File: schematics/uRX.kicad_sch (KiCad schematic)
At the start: 70 parts, among them J1 RF_In, J2 AudioJack2_Ground, J5 +5V, J6 RF_In, U1 CBT3253, U2 LM4562, U3 ESP32-DEVKIT, U4 Si5351A-B-GT, U5 OPA2690, U6 Si4732-A10, U7 PCM1808PWR, U8 LM4040-2.5, Y1 25MHz, Y2 32768kHz

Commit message: schematics finalization
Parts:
- removed C10, C11, C12: 100n, Capacitor_THT:C_Disc_D6.0mm_W2.5mm_P5.00mm, symbol Device:C_Small
- removed J2: AudioJack2_Ground, symbol Connector_Audio:AudioJack2_Ground
- removed L1, L2: Ferrite_perl, symbol Device:L_Ferrite_Small
- removed unit 3 of U2
- added C29: 10u, Capacitor_SMD:C_0603_1608Metric, symbol Device:C_Small
- added C30, C31: 100n, Capacitor_SMD:C_0603_1608Metric, symbol Device:C_Small
- added J3: AudioJack2_Ground, symbol Connector_Audio:AudioJack2_Ground
- added J4: +5Vfiltered, Connector_Pin:Pin_D0.9mm_L10.0mm_W2.4mm_FlatFork, symbol Connector_Generic:Conn_01x01
- added J7: +3.3Vfiltered, Connector_Pin:Pin_D0.9mm_L10.0mm_W2.4mm_FlatFork, symbol Connector_Generic:Conn_01x01
- added L5, L6: Ferrite_perl, Inductor_SMD:L_0603_1608Metric, symbol Device:L_Ferrite_Small
- added R22, R23, R24: 22, Resistor_SMD:R_0603_1608Metric, symbol Device:R
- added Rf1: 33, Resistor_SMD:R_0603_1608Metric, symbol Device:R
- added U9: PCM1808PWR, PW14, symbol 2026-01-28_13-06-42:PCM1808PWR
- C1, C13, C14, C17, C18, C20, C21, C22, C23, C25, C28, C8, C9: footprint Capacitor_THT:C_Disc_D3.8mm_W2.6mm_P2.50mm -> Capacitor_SMD:C_0603_1608Metric
- C15, C16, C19, C2, C24, C26, C27, C3, C4, C5: footprint Capacitor_THT:C_Disc_D6.0mm_W2.5mm_P5.00mm -> Capacitor_SMD:C_0603_1608Metric
- R1, R10, R11, R12, R13, R14, R16, R18, R19, R2, R20, R21, R3, R4, R5, R6, R8, Rf10, Rf8: footprint Resistor_THT:R_Axial_DIN0207_L6.3mm_D2.5mm_P10.16mm_Horizontal -> Resistor_SMD:R_0603_1608Metric
- U2, U5: footprint Package_DIP:DIP-8_W7.62mm_Socket_LongPads -> SOIC-8
- U6: footprint Package_SO:SOIC-16_3.9x9.9mm_P1.27mm -> Package_SO:SOIC-8_3.9x4.9mm_P1.27mm
- renumbered Rg10DNP to Rg10DNP1, Rg8DNP to Rg8DNP1
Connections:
- net +3.3V: now also L5.1; no longer U6.14 (VDD)
- net +5V: now also L6.1; no longer R20.2, U1.16 (VCC)
- net GND: now also C29.1, C30.1, C31.1, U9.10 (MD0), U9.11 (MD1), U9.12 (FMT), U9.2 (AGND), U9.5 (DGND); no longer C23.2, C28.2, U7.3 (VCC), U7.4 (VDD)
- net SCL: now also U6.11 (SCLK)
- net SDA: now also U6.12 (SDIO)
- net at C18.1: now also J3.S, U9.13 (VINL)
- net at C17.1: now also J3.T, U9.14 (VINR)
- net I2S0_DOUT: now reaches R21.2
- net I2S0_DOUT: now also U3.21 (D32)
- net at U4.6 (CLK2): now also Rf1.2; no longer U7.6 (SCKI)
- net I2S1_DOUT: now reaches U3.15 (D23)
- net I2S1_DOUT: now also R24.2
- net I2S1_LRCK: now reaches U3.23 (D25)
- net I2S1_LRCK: now also R22.2
- net I2S1_BCK: now reaches U3.24 (D26)
- net I2S1_BCK: now also R23.2
- net I2S0_BCK: now reaches U3.26 (D14)
- net I2S0_BCK: now also R2.2
- net I2S0_LRCK: now reaches U3.3 (D15)
- net I2S0_LRCK: now also R1.2
- net Pin8 V+ renamed +5Vfiltered
- net +5Vfiltered: now also C28.2, R20.2, U1.16 (VCC), U7.3 (VCC), C31.2, U9.3 (VCC)
- new net: J7.1 (Pin_1), L5.2
- new net: J4.1 (Pin_1), L6.2
- new net: R23.1, U9.8 (BCK)
- new net: C29.2, U9.1 (VREF)
- new net: R24.1, U9.9 (DOUT)
- new net: Rf1.1, U7.6 (SCKI), U9.6 (SCKI)
- new net: R22.1, U9.7 (LRCK)
- new net +3.3Vfiltered: C23.2, C30.2, U6.14 (VDD), U7.4 (VDD), U9.4 (VDD)
- no-connect marks 24 -> 17
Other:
- moved on the sheet: C17, C18, C20, C23, C25, C26, C27, C28, J6, R1, R2, R21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

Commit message: add usb power
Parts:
- removed R6: 10k, Resistor_SMD:R_0603_1608Metric, symbol Device:R
- added Bat1+: Bat1-, JST-XH, symbol Connector:Conn_01x02_Socket
- added Bat2+: Bat2-, JST-XH, symbol Connector:Conn_01x02_Socket
- added C10, C12: 2.2u, Capacitor_SMD:C_0603_1608Metric, symbol Device:C_Small
- added C11: 100n, Capacitor_SMD:C_0603_1608Metric, symbol Device:C_Small
- added D1: LED_Small, symbol Device:LED_Small
- added P1: USB_C_Plug_USB2.0, symbol Connector:USB_C_Plug_USB2.0
- added R25: 10kΩ, Resistor_SMD:R_0603_1608Metric, symbol Device:R_Small
- added R26, R6: 4.7kΩ, Resistor_SMD:R_0603_1608Metric, symbol Device:R_Small
- added Rf2, Rf3: 47, Resistor_SMD:R_0603_1608Metric, symbol Device:R
- added U11: IP2326, Package_DFN_QFN:QFN-24-1EP_4x4mm_P0.5mm_EP2.7x2.7mm, symbol uRX:STUSB4500QTR
- C25: value ... -> 100p
- C8, C9: value 1n -> 2.2u
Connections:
- net +3.3Vfiltered: now also R5.1
- net +5Vfiltered: now also C10.1, C11.1
- net GND: now also C9.2, C10.2, C11.2, C12.2, D1.1 (K), R25.2, R26.2, R6.2, U11.18 (PGND); no longer U7.11 (MD1), U9.11 (MD1)
- net at U3.19 (D34), U6.9 (RST): now also R5.2
- net at U3.5 (D4): no longer C9.2
- net VRev2.5: now reaches C26.1, C27.1, R18.2, R19.2, R20.1, U8.4 (K)
- new net: P1.A1 (GND), P1.A12 (GND), P1.B1 (GND), P1.B12 (GND)
- new net: P1.A4 (VBUS), P1.A9 (VBUS), P1.B4 (VBUS), P1.B9 (VBUS)
- new net: P1.A6 (D+), U11.2 (DP)
- new net: P1.A7 (D-), U11.1 (DM)
- new net: Rf2.1, U1.2 (S1)
- new net: Rf2.2, U4.9 (CLK1)
- new net: R26.1, U11.11 (ISET)
- new net: Bat1+.2 (Pin_2), Bat2+.2 (Pin_2), C9.1, U11.21 (VOUT), U11.22 (VOUT)
- new net: Bat1+.1 (Pin_1), Bat2+.1 (Pin_1)
- new net: D1.2 (A), U11.6 (LED)
- new net: R6.1, U11.3 (VSET)
- new net: Rf3.2, U4.10 (CLK0)
- new net: R25.1, U11.4 (NTC)
- new net: C12.1, U11.19 (VSYS), U11.20 (VSYS)
- new net: U11.25 (GND), U11.8 (VIN_UVSET)
- new net: Rf3.1, U1.14 (S0)
- now unconnected: C8.1, C8.2, U3.9 (D18)
- no-connect marks 17 -> 15
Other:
- moved on the sheet: C16, C25, C26, C27, C5, R10, R20, U8

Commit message: finalize power circuit
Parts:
- removed Bat1+: Bat1-, JST-XH, symbol Connector:Conn_01x02_Socket
- removed Bat2+: Bat2-, JST-XH, symbol Connector:Conn_01x02_Socket
- removed C9: 2.2u, Capacitor_SMD:C_0603_1608Metric, symbol Device:C_Small
- added Bat0, Bat1: JST-XH, symbol Connector_Generic:Conn_01x03
- added C32: 100n, Capacitor_SMD:C_0603_1608Metric, symbol Device:C_Small
- added C33: 4.7n, Capacitor_SMD:C_0603_1608Metric, symbol Device:C_Small
- added D2: LED_Small, symbol Device:LED_Small
- added L1: 2.2uH,50mA, PCM_JLCPCB:L_0805, symbol PCM_JLCPCB-Inductors:1uH,50mA
- added R27, R33: 100, Resistor_SMD:R_0603_1608Metric, symbol Device:R_Small
- added R28: 0.5, Resistor_SMD:R_0603_1608Metric, symbol Device:R_Small
- added R29: 5.1K, Resistor_SMD:R_0603_1608Metric, symbol Device:R_Small
- added R30: 51k, Resistor_SMD:R_0603_1608Metric, symbol Device:R_Small
- added R31, R32: 120K, Resistor_SMD:R_0603_1608Metric, symbol Device:R_Small
- added R4: 100, Resistor_SMD:R_0603_1608Metric, symbol Device:R
- C12, C8: value 2.2u -> 10u
- R25: value 10kΩ -> 1M
- R26: value 4.7kΩ -> 60K
- R6: value 4.7kΩ -> 5.1kΩ
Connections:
- net GND: now also C8.2, P1.A1 (GND), P1.A12 (GND), P1.B1 (GND), P1.B12 (GND), U11.24 (VBAT_GND), Bat0.1 (Pin_1), Bat1.1 (Pin_1), C33.2, D2.1 (K), R29.2, R30.2, R31.2, R32.2
- net at P1.A4 (VBUS), P1.A9 (VBUS), P1.B4 (VBUS)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: now also R28.1
- net at P1.A5 (CC): now also R6.1
- net at P1.S1 (SHIELD): now also R25.1, C33.1
- net at U11.21 (VOUT), U11.22 (VOUT): now also Bat0.3 (Pin_3), Bat1.3 (Pin_3)
- net at D1.2 (A): now also R27.2; no longer U11.6 (LED)
- net at U11.3 (VSET): no longer R6.1
- net at U11.4 (NTC): now also R30.1; no longer R25.1
- net at U11.13 (VIN): now also C8.1, L1.2, R28.2, R29.1
- net at U11.14 (BST): now also C32.2
- net at U11.15 (LX): now also U11.17 (LX)
- net at U11.16 (LX): now also C32.1, L1.1
- net at U11.23 (VBATM): now also R4.1
- net at U11.25 (GND), U11.8 (VIN_UVSET): now also R32.1
- net at U11.5 (BAT_STAT): now also R33.1
- net at U11.9 (VIN_OVSET): now also R31.1
- new net: Bat0.2 (Pin_2), Bat1.2 (Pin_2), R4.2
- new net: R27.1, U11.6 (LED)
- new net: D2.2 (A), R33.2
- no-connect marks 15 -> 19
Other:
- moved on the sheet: C12, C8, P1, R26

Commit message: add power to the rest
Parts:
- removed Bat0, Bat1: JST-XH, symbol Connector_Generic:Conn_01x03
- removed C12: 10u, Capacitor_SMD:C_0603_1608Metric, symbol Device:C_Small
- removed C25: 100p, Capacitor_SMD:C_0603_1608Metric, symbol Device:C_Small
- removed C32: 100n, Capacitor_SMD:C_0603_1608Metric, symbol Device:C_Small
- removed C33: 4.7n, Capacitor_SMD:C_0603_1608Metric, symbol Device:C_Small
- removed D1, D2: LED_Small, symbol Device:LED_Small
- removed J6: RF_In, Connector_Pin:Pin_D0.9mm_L10.0mm_W2.4mm_FlatFork, symbol Connector_Generic:Conn_01x01
- removed JP1: Conn_01x02_Male, Connector_PinHeader_2.00mm:PinHeader_1x02_P2.00mm_Vertical, symbol Connector:Conn_01x02_Male
- removed L1: 2.2uH,50mA, PCM_JLCPCB:L_0805, symbol PCM_JLCPCB-Inductors:1uH,50mA
- removed P1: USB_C_Plug_USB2.0, symbol Connector:USB_C_Plug_USB2.0
- removed R15: 2.0kΩ, Resistor_SMD:R_0603_1608Metric, symbol Device:R_Small
- removed R25: 1M, Resistor_SMD:R_0603_1608Metric, symbol Device:R_Small
- removed R26: 60K, Resistor_SMD:R_0603_1608Metric, symbol Device:R_Small
- removed R27, R33: 100, Resistor_SMD:R_0603_1608Metric, symbol Device:R_Small
- removed R28: 0.5, Resistor_SMD:R_0603_1608Metric, symbol Device:R_Small
- removed R29: 5.1K, Resistor_SMD:R_0603_1608Metric, symbol Device:R_Small
- removed R30: 51k, Resistor_SMD:R_0603_1608Metric, symbol Device:R_Small
- removed R31, R32: 120K, Resistor_SMD:R_0603_1608Metric, symbol Device:R_Small
- removed R4: 100, Resistor_SMD:R_0603_1608Metric, symbol Device:R
- removed R6: 5.1kΩ, Resistor_SMD:R_0603_1608Metric, symbol Device:R_Small
- removed R9: 10kΩ, Resistor_SMD:R_0603_1608Metric, symbol Device:R_Small
- removed U11: IP2326, Package_DFN_QFN:QFN-24-1EP_4x4mm_P0.5mm_EP2.7x2.7mm, symbol uRX:STUSB4500QTR
- added Bat2, Bat3: JST-XH, Connector_JST:JST_XH_B3B-XH-A_1x03_P2.50mm_Vertical, symbol uRX:Conn_01x03
- added C34, C36, C37: 10u, Capacitor_SMD:C_0603_1608Metric, symbol uRX:C_Small
- added C35: 100n, Capacitor_SMD:C_0603_1608Metric, symbol uRX:C_Small
- added C9: 4.7n, Capacitor_SMD:C_0603_1608Metric, symbol uRX:C_Small
- added D3, D4: LED_Small, LED_SMD:L_0603_1608Metric, symbol uRX:LED_Small
- added J2: USB_C_Receptacle_USB2.0_14P, C165948, symbol uRX:USB_C_Receptacle_USB2.0_14P
- added J8: RF_In, Connector_Pin:Pin_D0.9mm_L10.0mm_W2.4mm_FlatFork, symbol Connector_Generic:Conn_01x01
- added L2: 2.2uH,3A, Inductor_SMD:L_4.0x4.0_H1.8, symbol uRX:1uH,50mA
- added R34: 1M, Resistor_SMD:R_0603_1608Metric, symbol uRX:R_Small
- added R35, R36, R44: 5.1K, Resistor_SMD:R_0603_1608Metric, symbol uRX:R_Small
- added R37: 33k, Resistor_SMD:R_0603_1608Metric, symbol uRX:R_Small
- added R38, R40: 100, Resistor_SMD:R_0603_1608Metric, symbol uRX:R_Small
- added R39: 100, Resistor_SMD:R_0603_1608Metric, symbol uRX:R
- added R41, R42: 120K, Resistor_SMD:R_0603_1608Metric, symbol uRX:R_Small
- added R43: 75k, Resistor_SMD:R_0603_1608Metric, symbol uRX:R_Small
- added U10: IP2326, Package_DFN_QFN:QFN-24-1EP_4x4mm_P0.5mm_EP2.7x2.7mm, symbol uRX:IP2326
- C8: value 10u -> 100p
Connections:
- net +5V: no longer J5.1 (Pin_1)
- net +5Vfiltered: now also C10.2, C11.2, C13.2, C14.2, C19.2, C2.2, C20.1, C20.2, C21.1, C22.1, C23.1, C24.2, C26.2, C27.2, C28.1, C29.1, C29.2, C3.2, C30.1, C31.1, C4.2, C5.2, R16.2, Rg10DNP1.2, Rg8DNP1.2, U1.1 (1~{OE}), U1.15 (2~{OE}), U1.8 (GND), U3.2 (GND), U3.29 (GND), U4.8 (GND), U6.10 (SENB), U6.15 (GND), U7.1 (VREF), U7.10 (MD0), U7.11 (MD1), U7.12 (FMT), U7.2 (AGND), U7.5 (DGND), U8.5 (A), U9.1 (VREF), U9.10 (MD0), U9.11 (MD1), U9.12 (FMT), U9.2 (AGND), U9.5 (DGND), Bat2.1 (Pin_1), Bat3.1 (Pin_1), C34.2, C36.2, C37.2, C9.2, D3.1 (K), D4.1 (K), J2.A1 (GND), J2.A12 (GND), J2.B1 (GND), J2.B12 (GND), R34.2, R35.2, R36.2, R37.2, R41.2, R42.2, R43.2, R44.2, U10.18 (PGND), U10.24 (VBAT_GND)
- net at U6.6 (FMI): now also C8.1
- net at R14.1, U6.8 (AMI): now also Rf3.1, U1.14 (S0)
- removed net GND: C10.2, C11.2, C13.2, C14.2, C19.2, C2.2, C20.1, C21.1, C22.1, C23.1, C24.2, C26.2, C27.2, C28.1, C29.1, C3.2, C30.1, C31.1, C4.2, C5.2, C8.2, R16.2, Rg10DNP1.2, Rg8DNP1.2, U1.1 (1~{OE}), U1.15 (2~{OE}), U1.8 (GND), U3.2 (GND), U3.29 (GND), U4.8 (GND), U6.15 (GND), U7.10 (MD0), U7.12 (FMT), U7.2 (AGND), U7.5 (DGND), U8.5 (A), U9.10 (MD0), U9.12 (FMT), U9.2 (AGND), U9.5 (DGND)
- new net: C37.1, U10.20 (VSYS)
- new net: C34.1, J2.A4 (VBUS), J2.A9 (VBUS), J2.B4 (VBUS), J2.B9 (VBUS), L2.2, R44.1, U10.12 (EN), U10.13 (VIN)
- new net: J2.A5 (CC1), R36.1
- new net: J2.A6 (D+), J2.B6 (D+), U10.2 (DP)
- new net: J2.A7 (D-), J2.B7 (D-), U10.1 (DM)
- new net: J2.B5 (CC2), R35.1
- new net: C9.1, J2.S1 (SHIELD), R34.1
- new net: D4.2 (A), R40.2
- new net: Bat2.2 (Pin_2), Bat3.2 (Pin_2), R39.2
- new net: Bat2.3 (Pin_3), Bat3.3 (Pin_3), U10.21 (VOUT), U10.22 (VOUT)
- new net: R42.1, U10.9 (VIN_OVSET)
- new net: R43.1, U10.11 (ISET)
- new net: C35.2, U10.14 (BST)
- new net: U10.15 (LX), U10.17 (LX)
- new net: C35.1, L2.1, U10.16 (LX)
- new net: C36.1, U10.19 (VSYS)
- new net: R39.1, U10.23 (VBATM)
- new net: R41.1, U10.25 (GND), U10.8 (VIN_UVSET)
- new net: R37.1, U10.4 (NTC)
- new net: R38.1, U10.5 (BAT_STAT)
- new net: R40.1, U10.6 (LED)
- new net: C8.2, J8.1 (Pin_1)
- new net: D3.2 (A), R38.2
- no-connect marks 19 -> 18
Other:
- note removed: "I2C Addr Select"
- moved on the sheet: C1, C10, C11, C13, C14, C15, C16, C17, C18, C19, C2, C20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

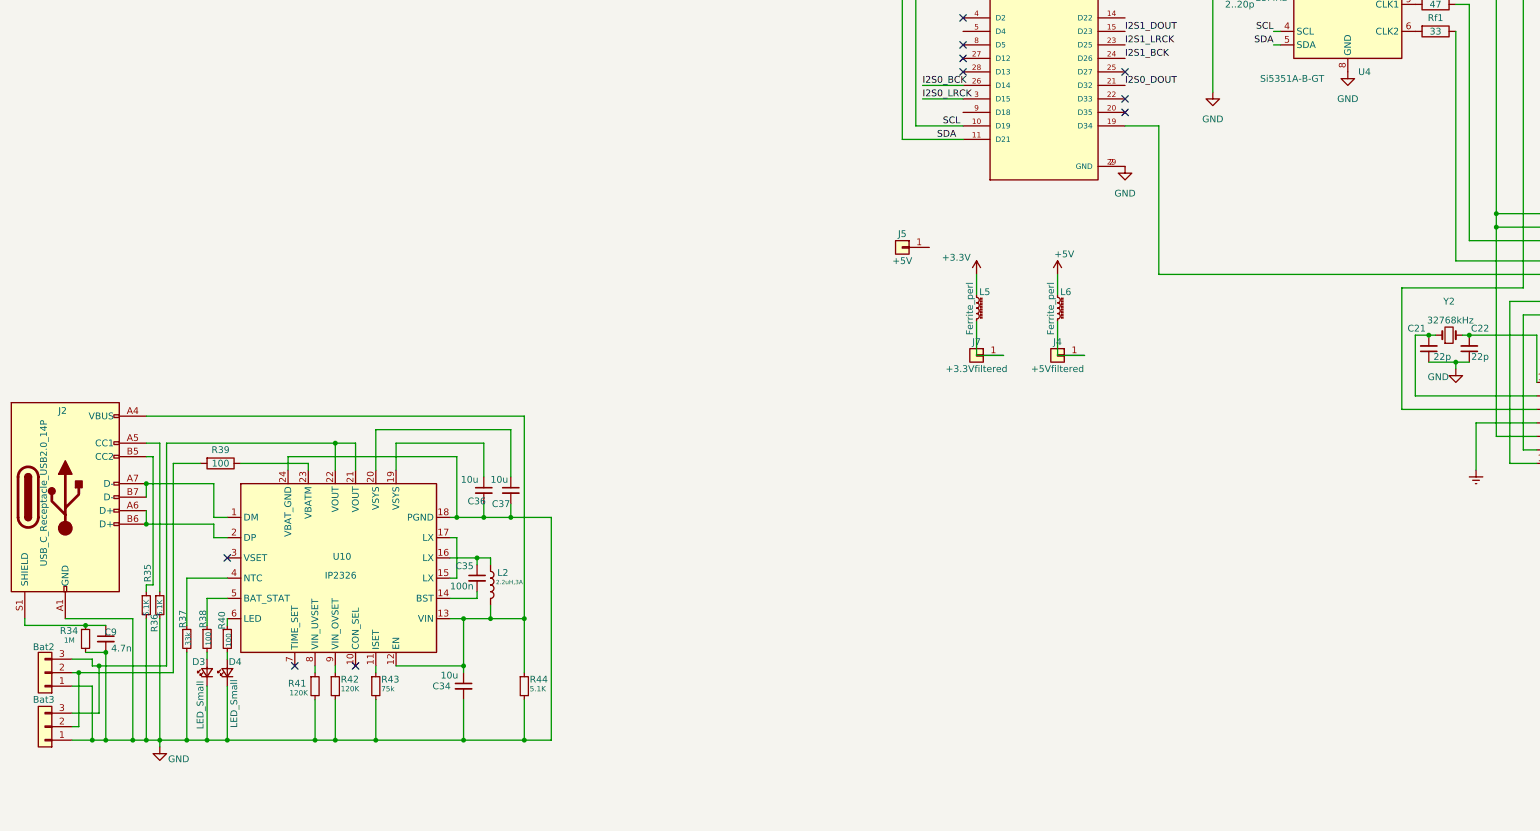
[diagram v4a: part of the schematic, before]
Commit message: gpio to vbat_stat
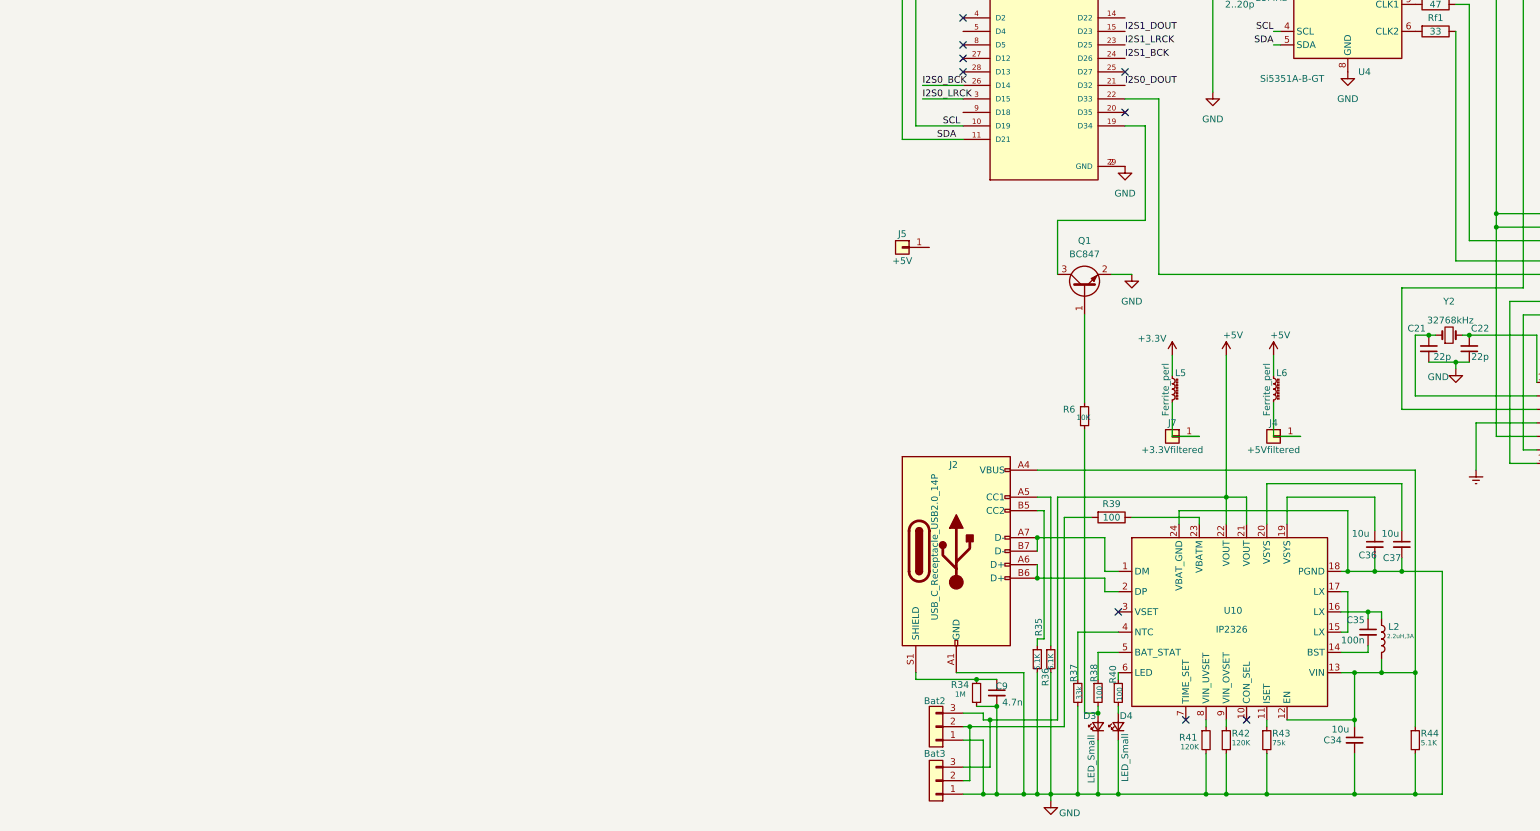
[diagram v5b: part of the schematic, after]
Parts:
- added Q1: BC847, Package_TO_SOT_SMD:SOT-23, symbol Transistor_BJT:BC847
- added R6: 10K, Resistor_SMD:R_0603_1608Metric, symbol Device:R_Small
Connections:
- net +5V: now also Bat2.3 (Pin_3), Bat3.3 (Pin_3), U10.21 (VOUT), U10.22 (VOUT)
- net +5Vfiltered: now also Q1.2 (E)
- net at R5.2, U6.9 (RST): now also U3.22 (D33); no longer U3.19 (D34)
- net at D3.2 (A), R38.2: now also R6.2
- new net: Q1.1 (B), R6.1
- new net: Q1.3 (C), U3.19 (D34)
- no-connect marks 18 -> 17
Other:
- moved on the sheet: Bat2, Bat3, C34, C35, C36, C37, C9, D3, D4, J2, J4, J7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
